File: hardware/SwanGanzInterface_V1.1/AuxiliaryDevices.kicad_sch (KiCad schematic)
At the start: 25 parts, among them IC1 TSC2046IPWR, J10 Conn_01x05_Pin, J12 Conn_01x06_Pin, J8 1051640001, U6 FT232RL

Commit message: Schematic Check
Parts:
- removed J10: Conn_01x05_Pin, symbol Connector:Conn_01x05_Pin
- added C37: 1u, symbol Device:C
- added J10, J8: Conn_01x04_Pin, symbol Connector:Conn_01x04_Pin
- added R38: 0, symbol Device:R
- U11: renamed from U6; value FT232RL -> FT232RNL
- renumbered C31 to C27, C25 to C28, C26 to C29, C27 to C30, C32 to C31, D5 to D1, D7 to D2, D8 to D3, D6 to D5, IC1 to IC2, J12 to J11, J8 to J9, R39 to R36, R11 to R37, R46 to R39, R47 to R40, R1 to R43, R2 to R44, R43 to R45
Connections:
- net +3V3: now also C37.1, R38.2
- net GND: now also C37.2, J10.4 (Pin_4), J8.4 (Pin_4)
- net MICRO_VBUS: now also J8.1 (Pin_1)
- net MSP_RX_PA9_FT232_TX: now also J10.2 (Pin_2); no longer U11.1 (TXD)
- net MSP_TX_PA8_FT232_RX: now also J10.3 (Pin_3); no longer U11.5 (RXD)
- net USB_D+: now also J8.2 (Pin_2)
- net USB_D-: now also J8.3 (Pin_3)
- net FT232R_RST renamed FT_RST_PA29
- net USB_CONN_PA10 renamed USB_CONN_PA30
- net USB_MSP_CTS_PB2_RS232_RTS renamed MSP_CTS_PB26_FT_RTS
- net USB_MSP_RTS_PB3_RS232_CTS renamed MSP_RTS_PB25_FT_CTS
- new net: J10.1 (Pin_1), R38.1
- new net MSP_RX_PA1_FT_TX: U11.1 (TXD)
- new net MSP_TX_PA28_FT_RX: U11.5 (RXD)
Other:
- note added: "Auxilary Devices"
- note added: "Blue"
- note added: "Decoupling Caps for FT232RNL Internal Regulator"
- note added: "FT232 Status LEDs"
- note added: "FT232RNL Data Sheet says to have caps on D+/D- to ground this seems stupid though"
- note added: "For power and desktop app communcation"
- note added: "Green"
- note added: "In case MicroUSB_VBUS is removed"
- note added: "Red"
- note added: "Resistive Touch Screen Controller"
- note added: "UART Debugging Pins"
- note added: "UART to USB Converter"
- note added: "USB Connected"
- note added: "When MICRO_VBUS = 5V USB_CONN = (19.4k * 5V) / (19.4k * 10k) = 3.3V Logic High"
- note removed: "Data Sheet says to have caps on D+/D- This seems stupid though"
- moved on the sheet: C27, C29, C30, C31, D4, D5, IC2, J11, J9, JP1, R36, R41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

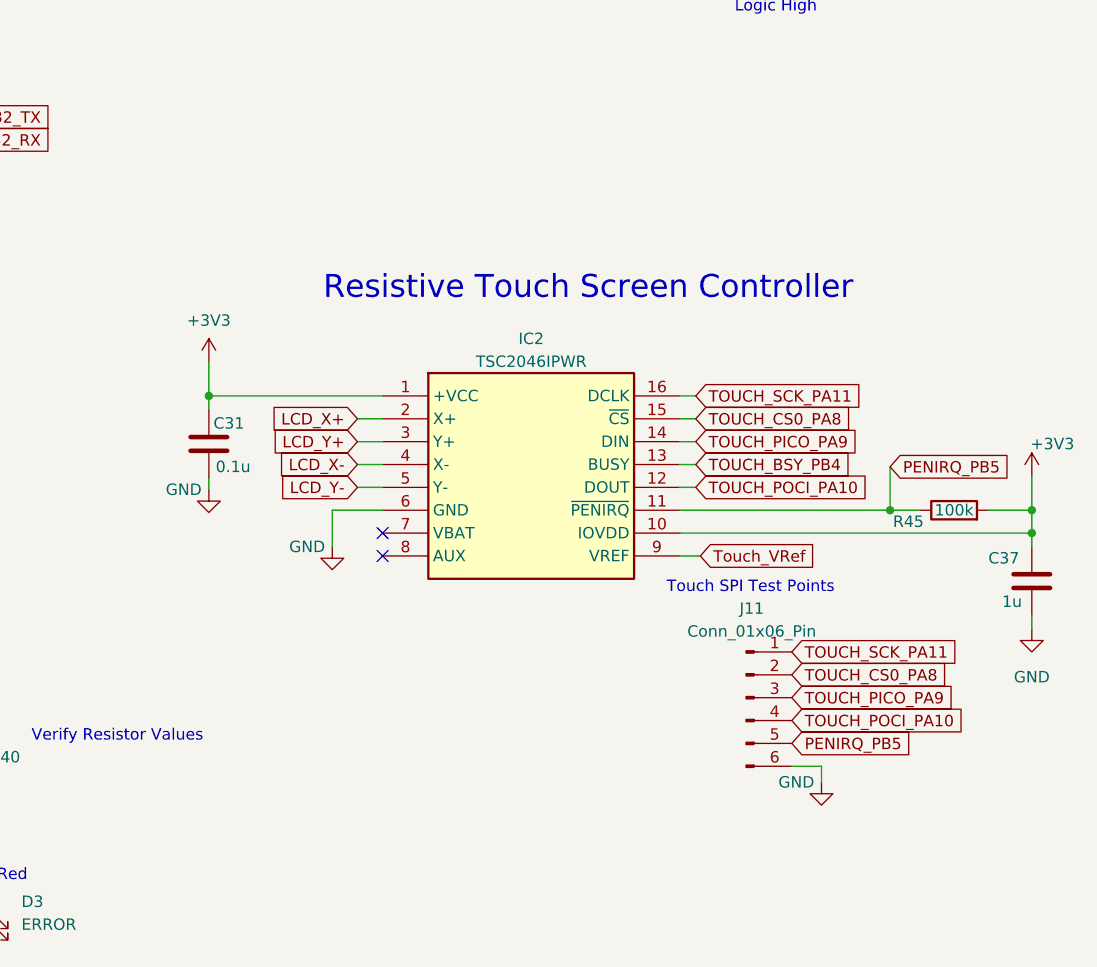
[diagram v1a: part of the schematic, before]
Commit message: Filter paramaters and assigned footprints
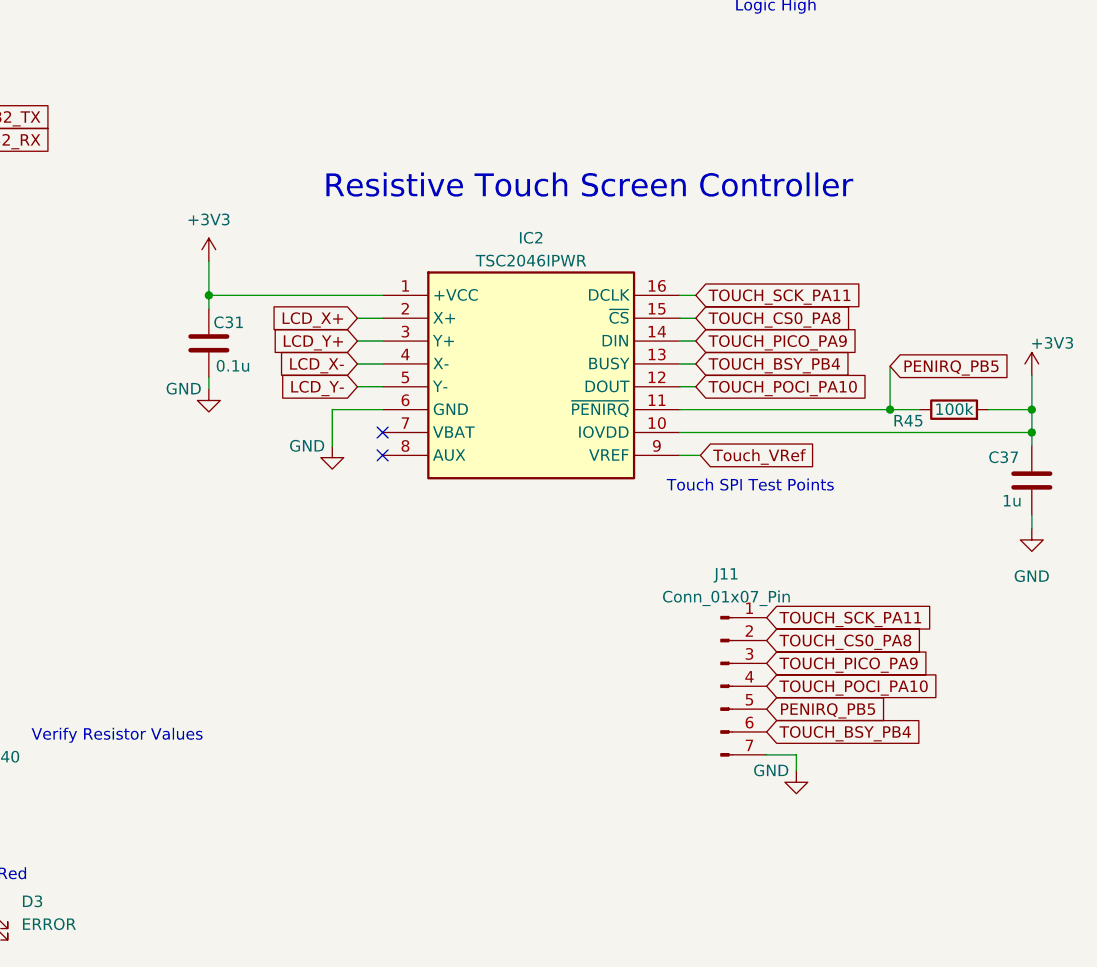
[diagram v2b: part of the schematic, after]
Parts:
- removed J11: Conn_01x06_Pin, symbol Connector:Conn_01x06_Pin
- added J11: Conn_01x07_Pin, Connector_PinHeader_2.54mm:PinHeader_1x07_P2.54mm_Vertical, symbol Connector:Conn_01x07_Pin
- C27, C28, C29, C31, C37: footprint (none) -> Capacitor_SMD:C_0603_1608Metric
- C30: footprint (none) -> Capacitor_SMD:C_0805_2012Metric
- J10, J8: footprint (none) -> Connector_PinHeader_2.54mm:PinHeader_1x04_P2.54mm_Vertical
- R36, R38, R41, R42, R43, R44, R45: footprint (none) -> Resistor_SMD:R_0603_1608Metric
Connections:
- net GND: now also J11.7 (Pin_7)
- net PENIRQ_PB5: now also J11.5 (Pin_5)
- net TOUCH_BSY_PB4: now also J11.6 (Pin_6)
- net TOUCH_CS0_PA8: now also J11.2 (Pin_2)
- net TOUCH_PICO_PA9: now also J11.3 (Pin_3)
- net TOUCH_POCI_PA10: now also J11.4 (Pin_4)
- net TOUCH_SCK_PA11: now also J11.1 (Pin_1)
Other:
- moved on the sheet: C31, C37, IC2, R45

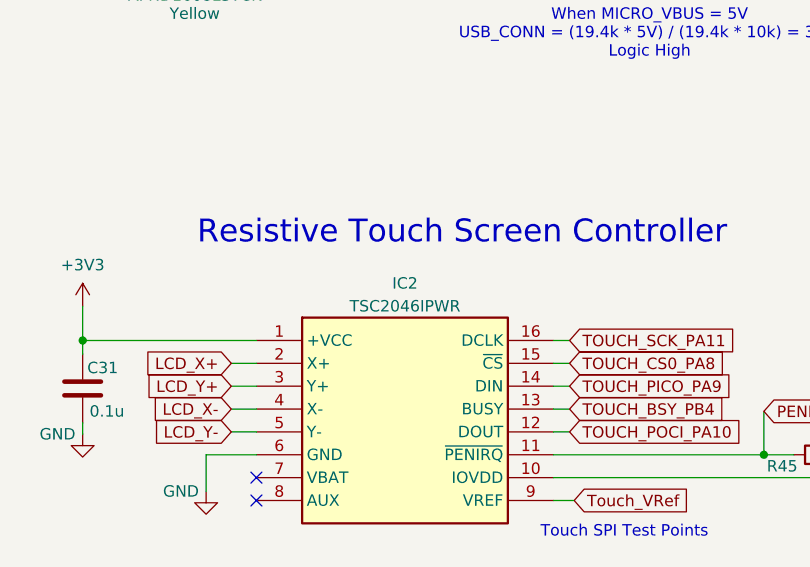
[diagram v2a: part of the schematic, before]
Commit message: Layout work on screen and expanded board size
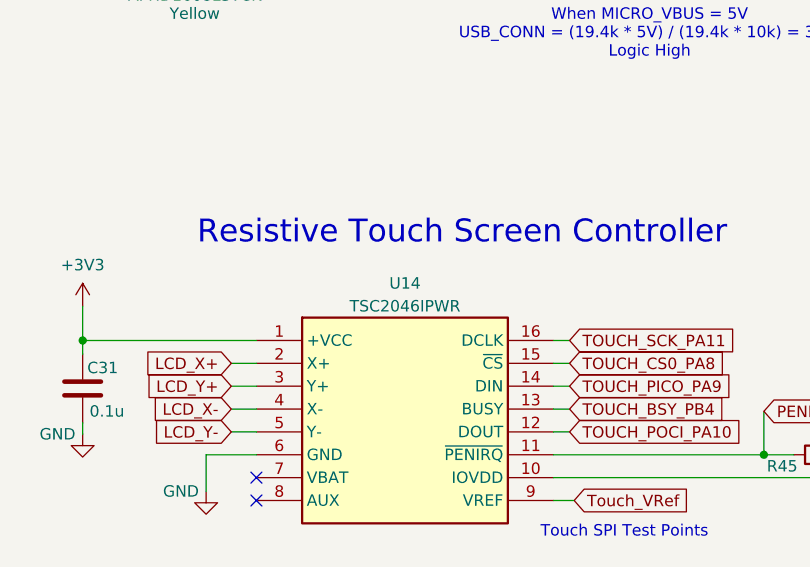
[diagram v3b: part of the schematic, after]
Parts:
- renumbered IC2 to U14
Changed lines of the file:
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@@
 		(on_board yes)
 		(dnp no)
-		(property "Reference" "IC2"
+		(property "Reference" "U14"
 			(at 223.52 101.092 0)
 			(effects
@@
 			(project "SwanGanzInterface_V1.1"
 				(path "/4e9a6e30-f660-472b-9696-bea1f34b4545/2a61924c-1b61-4422-811f-a61fd6f6c556"
-					(reference "IC2")
+					(reference "U14")
 					(unit 1)
 				)

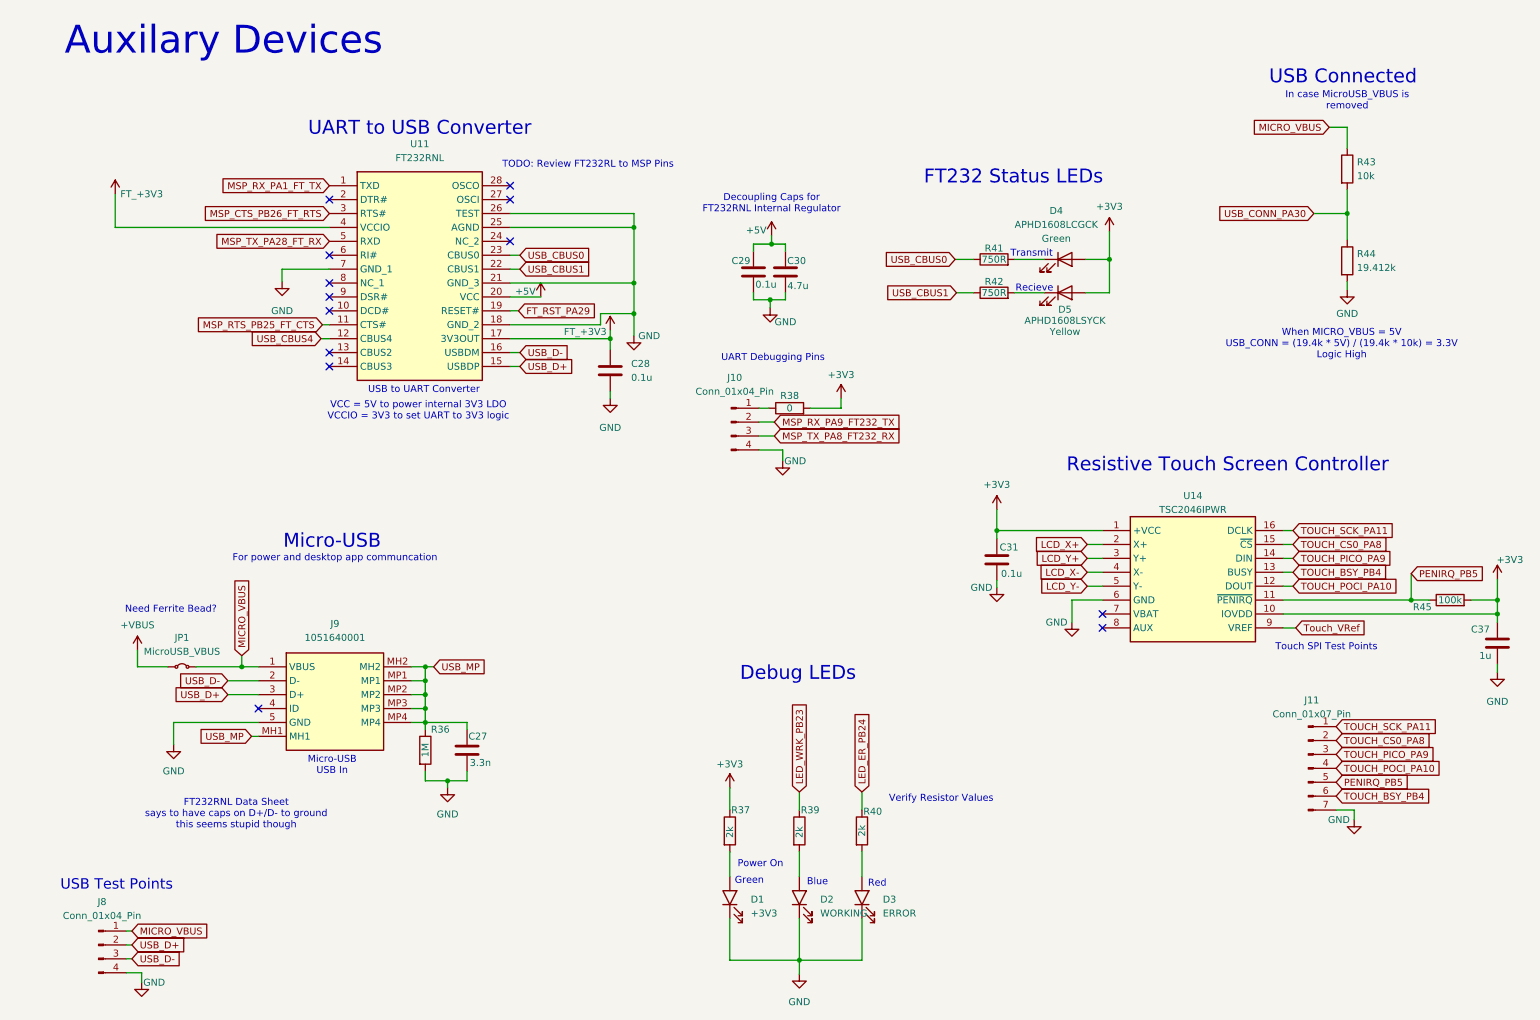
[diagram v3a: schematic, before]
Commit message: Button pin allocation, layout of power and ft, general layout
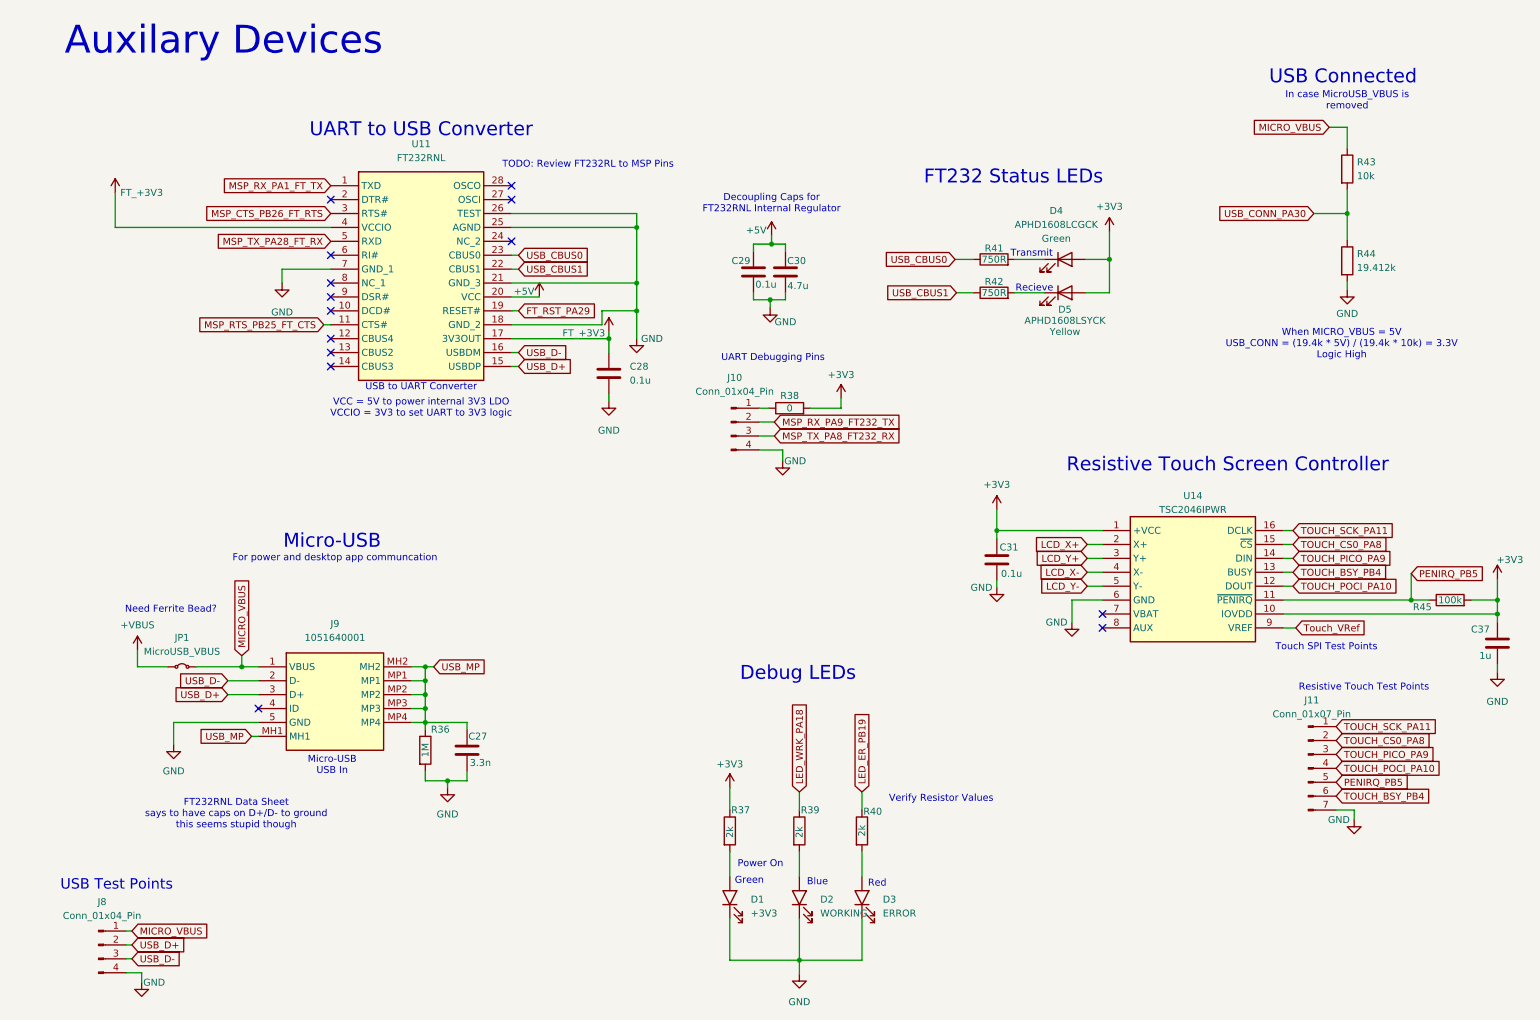
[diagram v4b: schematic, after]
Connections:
- net LED_ER_PB24 renamed LED_ER_PB19
- net LED_WRK_PB23 renamed LED_WRK_PA18
- net USB_CBUS4: no longer names the net of U11.12 (CBUS4)
- no-connect marks 13 -> 14
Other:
- note added: "Resistive Touch Test Points"
- moved on the sheet: C28
